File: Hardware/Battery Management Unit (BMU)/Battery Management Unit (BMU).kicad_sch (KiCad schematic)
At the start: 23 parts, among them J1 HIGH SIDE, J10 SHUNT, J11 ALERT, J12 CAN, J2 LOW SIDE, J3 POWER, J4 GPIO, J5 GND, J6 5V, J7 3V3, J8 FAULT, J9 I2C

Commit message: Both boards are now fully completed: the BMU and CMU.
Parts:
- TP1, TP10, TP11, TP2, TP3, TP4, TP5, TP6, TP7, TP8, TP9: symbol Connector:TestPoint_Small -> Connector:TestPoint_Square
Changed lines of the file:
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@@
 	)
 	(symbol
-		(lib_id "Connector:TestPoint_Small")
+		(lib_id "Connector:TestPoint_Square")
 		(at 240.03 153.67 0)
 		(unit 1)
@@
 		(in_pos_files yes)
 		(dnp no)
-		(fields_autoplaced yes)
 		(property "Reference" "TP3"
-			(at 241.3 152.3999 0)
+			(at 241.046 152.654 0)
 			(show_name no)
 			(do_not_autoplace no)
@@
 			)
 		)
-		(property "Datasheet" ""
+		(property "Datasheet" "~"
 			(at 245.11 153.67 0)
 			(hide yes)
@@
 	)
 	(symbol
-		(lib_id "Connector:TestPoint_Small")
+		(lib_id "Connector:TestPoint_Square")
 		(at 280.67 130.81 0)
 		(unit 1)
@@
 		(in_pos_files yes)
 		(dnp no)
-		(fields_autoplaced yes)
 		(property "Reference" "TP10"
-			(at 281.94 129.5399 0)
+			(at 281.686 129.794 0)
 			(show_name no)
 			(do_not_autoplace no)
@@
 			)
 		)
-		(property "Datasheet" ""
+		(property "Datasheet" "~"
 			(at 285.75 130.81 0)
 			(hide yes)
@@
 	)
 	(symbol
-		(lib_id "Connector:TestPoint_Small")
+		(lib_id "Connector:TestPoint_Square")
 		(at 279.4199 173.99 0)
 		(unit 1)
@@
 		(in_pos_files yes)
 		(dnp no)
-		(fields_autoplaced yes)
 		(property "Reference" "TP8"
-			(at 280.6899 172.7199 0)
+			(at 280.416 173.228 0)
 			(show_name no)
 			(do_not_autoplace no)
@@
 			)
 		)
-		(property "Datasheet" ""
+		(property "Datasheet" "~"
 			(at 284.4999 173.99 0)
 			(hide yes)
@@
 	)
 	(symbol
-		(lib_id "Connector:TestPoint_Small")
+		(lib_id "Connector:TestPoint_Square")
 		(at 279.4 165.1 0)
 		(unit 1)
@@
 		(in_pos_files yes)
 		(dnp no)
-		(fields_autoplaced yes)
 		(property "Reference" "TP6"
-			(at 280.67 163.8299 0)
+			(at 280.416 164.084 0)
 			(show_name no)
 			(do_not_autoplace no)
@@
 			)
 		)
-		(property "Datasheet" ""
+		(property "Datasheet" "~"
 			(at 284.48 165.1 0)
 			(hide yes)
@@
 	)
 	(symbol
-		(lib_id "Connector:TestPoint_Small")
+		(lib_id "Connector:TestPoint_Square")
 		(at 280.6355 135.89 0)
 		(unit 1)
@@
 		(in_pos_files yes)
 		(dnp no)
-		(fields_autoplaced yes)
 		(property "Reference" "TP9"
-			(at 281.9055 134.6199 0)
+			(at 281.94 134.874 0)
 			(show_name no)
 			(do_not_autoplace no)
@@
 			)
 		)
-		(property "Datasheet" ""
+		(property "Datasheet" "~"
 			(at 285.7155 135.89 0)
 			(hide yes)
@@
 	)
 	(symbol
-		(lib_id "Connector:TestPoint_Small")
+		(lib_id "Connector:TestPoint_Square")
 		(at 279.4 171.45 0)
 		(unit 1)
@@
 		(in_pos_files yes)
 		(dnp no)
-		(fields_autoplaced yes)
 		(property "Reference" "TP7"
-			(at 280.67 170.1799 0)
+			(at 280.416 170.434 0)
 			(show_name no)
 			(do_not_autoplace no)
@@
 			)
 		)
-		(property "Datasheet" ""
+		(property "Datasheet" "~"
 			(at 284.48 171.45 0)
 			(hide yes)
@@
 	)
 	(symbol
-		(lib_id "Connector:TestPoint_Small")
+		(lib_id "Connector:TestPoint_Square")
 		(at 279.3877 167.64 0)
 		(unit 1)
@@
 		(in_pos_files yes)
 		(dnp no)
-		(fields_autoplaced yes)
 		(property "Reference" "TP5"
-			(at 280.6577 166.3699 0)
+			(at 280.416 166.624 0)
 			(show_name no)
 			(do_not_autoplace no)
@@
 			)
 		)
-		(property "Datasheet" ""
+		(property "Datasheet" "~"
 			(at 284.4677 167.64 0)
 			(hide yes)
@@
 	)
 	(symbol
-		(lib_id "Connector:TestPoint_Small")
+		(lib_id "Connector:TestPoint_Square")
 		(at 240.03 144.78 0)
 		(unit 1)
@@
 		(in_pos_files yes)
 		(dnp no)
-		(fields_autoplaced yes)
 		(property "Reference" "TP2"
-			(at 241.3 143.5099 0)
+			(at 241.3 143.764 0)
 			(show_name no)
 			(do_not_autoplace no)
@@
 			)
 		)
-		(property "Datasheet" ""
+		(property "Datasheet" "~"
 			(at 245.11 144.78 0)
 			(hide yes)
@@
 	)
 	(symbol
-		(lib_id "Connector:TestPoint_Small")
+		(lib_id "Connector:TestPoint_Square")
 		(at 280.67 133.35 0)
 		(unit 1)
@@
 		(in_pos_files yes)
 		(dnp no)
-		(fields_autoplaced yes)
 		(property "Reference" "TP11"
-			(at 281.94 132.0799 0)
+			(at 281.686 132.334 0)
 			(show_name no)
 			(do_not_autoplace no)
@@
 			)
 		)
-		(property "Datasheet" ""
+		(property "Datasheet" "~"
 			(at 285.75 133.35 0)
 			(hide yes)
@@
 	)
 	(symbol
-		(lib_id "Connector:TestPoint_Small")
+		(lib_id "Connector:TestPoint_Square")
 		(at 240.03 142.24 0)
 		(unit 1)
@@
 		(in_pos_files yes)
 		(dnp no)
-		(fields_autoplaced yes)
 		(property "Reference" "TP1"
-			(at 241.3 140.9699 0)
+			(at 241.3 140.97 0)
 			(show_name no)
 			(do_not_autoplace no)
@@
 			)
 		)
-		(property "Datasheet" ""
+		(property "Datasheet" "~"
 			(at 245.11 142.24 0)
 			(hide yes)
@@
 	)
 	(symbol
-		(lib_id "Connector:TestPoint_Small")
+		(lib_id "Connector:TestPoint_Square")
 		(at 279.3064 177.8 0)
 		(unit 1)
@@
 		(in_pos_files yes)
 		(dnp no)
-		(fields_autoplaced yes)
 		(property "Reference" "TP4"
-			(at 280.5764 176.5299 0)
+			(at 280.162 176.784 0)
 			(show_name no)
 			(do_not_autoplace no)
@@
 			)
 		)
-		(property "Datasheet" ""
+		(property "Datasheet" "~"
 			(at 284.3864 177.8 0)
 			(hide yes)

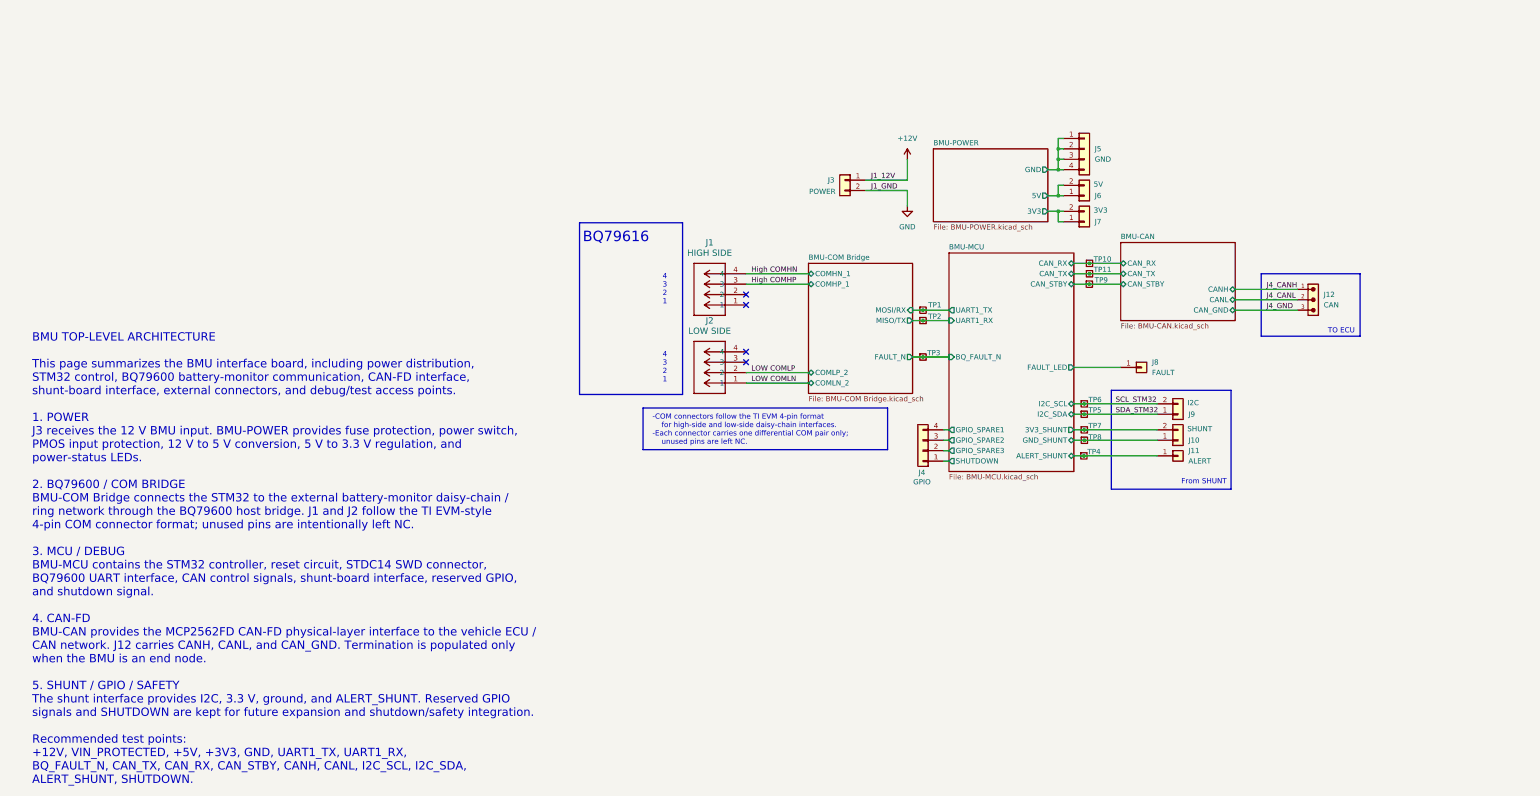
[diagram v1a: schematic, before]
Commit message: Schematic polish -- fixed to best standards, cleaned up for ERCs, etc
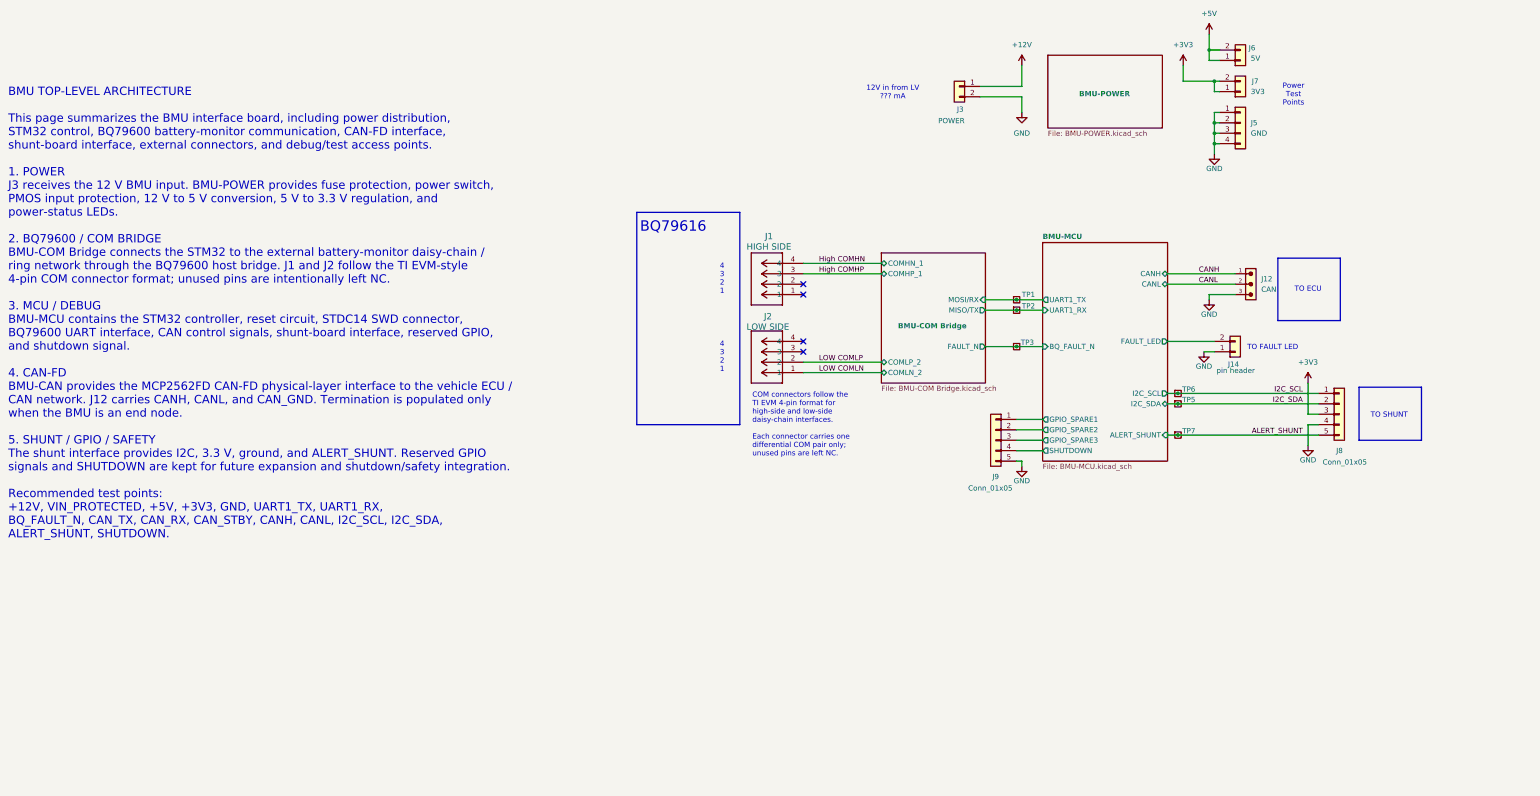
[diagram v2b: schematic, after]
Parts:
- removed J10: SHUNT, Connector_PinHeader_2.54mm:PinHeader_1x02_P2.54mm_Vertical, symbol Connector_Generic:Conn_01x02
- removed J11: ALERT, Connector_PinHeader_2.54mm:PinHeader_1x01_P2.54mm_Vertical, symbol Connector_Generic:Conn_01x01
- removed J4: GPIO, Connector_PinHeader_2.54mm:PinHeader_1x04_P2.54mm_Vertical, symbol Connector_Generic:Conn_01x04
- removed J8: FAULT, Connector_PinHeader_2.54mm:PinHeader_1x01_P2.54mm_Vertical, symbol Connector_Generic:Conn_01x01
- removed J9: I2C, Connector_PinHeader_2.54mm:PinHeader_1x02_P2.54mm_Vertical, symbol Connector_Generic:Conn_01x02
- removed TP10, TP11, TP4, TP8, TP9: TestPoint_Small, TestPoint:TestPoint_THTPad_D1.5mm_Drill0.7mm, symbol Connector:TestPoint_Square
- added J14: pin header, Connector_PinHeader_2.54mm:PinHeader_1x02_P2.54mm_Vertical, symbol Connector_Generic:Conn_01x02
- added J8, J9: Conn_01x05, symbol Connector_Generic:Conn_01x05
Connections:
- net BMU-POWER/GND is gone; now on net GND: J5.1 (Pin_1), J5.2 (Pin_2), J5.3 (Pin_3), J5.4 (Pin_4)
- net J4_GND is gone; now on net GND: J12.3
- net BMU-MCU/FAULT_LED: now also J14.2 (Pin_2)
- net BMU-MCU/GPIO_SPARE1: now also J9.1 (Pin_1)
- net BMU-MCU/GPIO_SPARE2: now also J9.2 (Pin_2)
- net BMU-MCU/GPIO_SPARE3: now also J9.3 (Pin_3)
- net BMU-MCU/SHUTDOWN: now also J9.4 (Pin_4)
- net GND: now also J14.1 (Pin_1), J8.4 (Pin_4), J9.5 (Pin_5)
- net BMU-MCU/3V3_SHUNT renamed ALERT_SHUNT
- net ALERT_SHUNT: now also J8.5 (Pin_5)
- net BMU-POWER/3V3 renamed +3V3
- net +3V3: now also J8.3 (Pin_3)
- net BMU-POWER/5V renamed +5V
- net J4_CANH renamed CANH
- net J4_CANL renamed CANL
- net SCL_STM32 renamed I2C_SCL
- net I2C_SCL: now also J8.1 (Pin_1)
- net SDA_STM32 renamed I2C_SDA
- net I2C_SDA: now also J8.2 (Pin_2)
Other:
- removed sheet BMU-CAN
- sheet BMU-MCU ports: added CANH, CANL; removed 3V3_SHUNT, CAN_RX, CAN_STBY, CAN_TX, GND_SHUNT
- sheet BMU-POWER ports: added none; removed 3V3, 5V, GND
- note added: "12V in from LV ??? mA"
- note added: "COM connectors follow the TI EVM 4-pin format for high-side and low-side daisy-chain interfaces. Each connector carries one differential COM pair only; unused pins are left NC."
- note added: "Power Test Points"
- note added: "TO FAULT LED"
- note added: "TO SHUNT"
- note removed: "-COM connectors follow the TI EVM 4-pin format for high-side and low-side daisy-chain interfaces. -Each connector carries one differential COM pair only; unused pins are left NC."
- note removed: "From SHUNT"
- moved on the sheet: J1, J12, J2, J3, J5, J6, J7, TP1, TP2, TP3, TP5, TP6

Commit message: update libraries+bmu
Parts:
- J1, J2: footprint 705510038:CONN_70551-xxxx_04_MOL -> Footprints:705510038
- J10: renamed from J8; value Conn_01x05 -> SHUNT; footprint (none) -> Connector_PinHeader_2.54mm:PinHeader_1x05_P2.54mm_Vertical
- J4: renamed from J9; value Conn_01x05 -> GPIO; footprint (none) -> Connector_PinHeader_2.54mm:PinHeader_1x05_P2.54mm_Vertical
- J9: renamed from J12; footprint 691382000003:691382000003 -> Footprints:691382000003
- renumbered J6 to J5, J7 to J6, J5 to J7, J14 to J8, TP5 to TP4, TP6 to TP5, TP7 to TP6
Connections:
- net +3V3: now also J10.1 (Pin_1); no longer J10.3 (Pin_3)
- net ALERT_SHUNT: now also J10.4 (Pin_4); no longer J10.5 (Pin_5)
- net GND: now also J10.5 (Pin_5); no longer J10.4 (Pin_4)
- net I2C_SCL: now also J10.3 (Pin_3); no longer J10.1 (Pin_1)
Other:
- moved on the sheet: J1, J10, J2, J3, J4, J5, J6, J7, J8, J9, TP1, TP2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

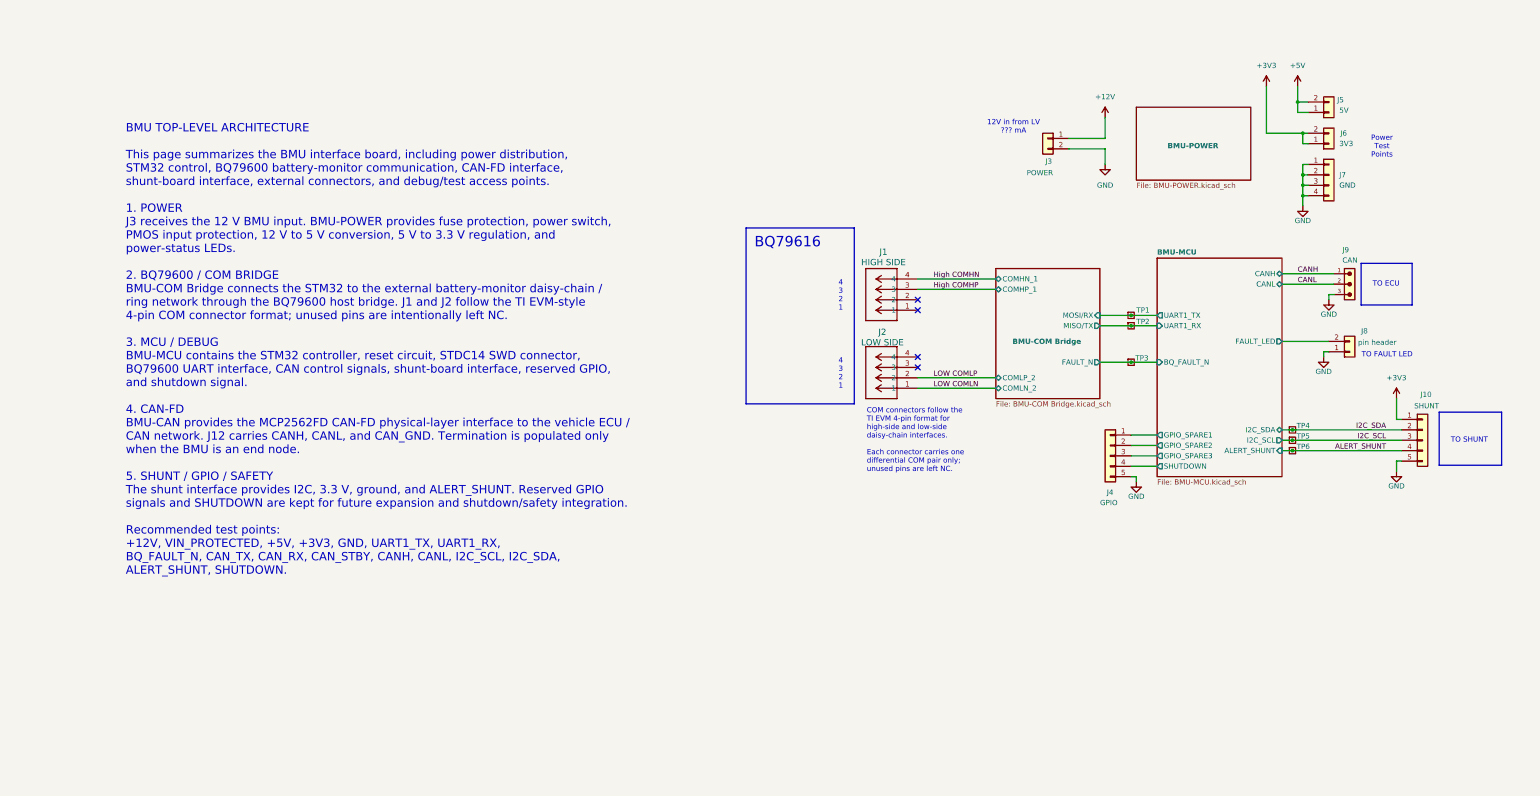
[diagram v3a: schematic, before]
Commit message: Schematic cleanup; lots of missing library files
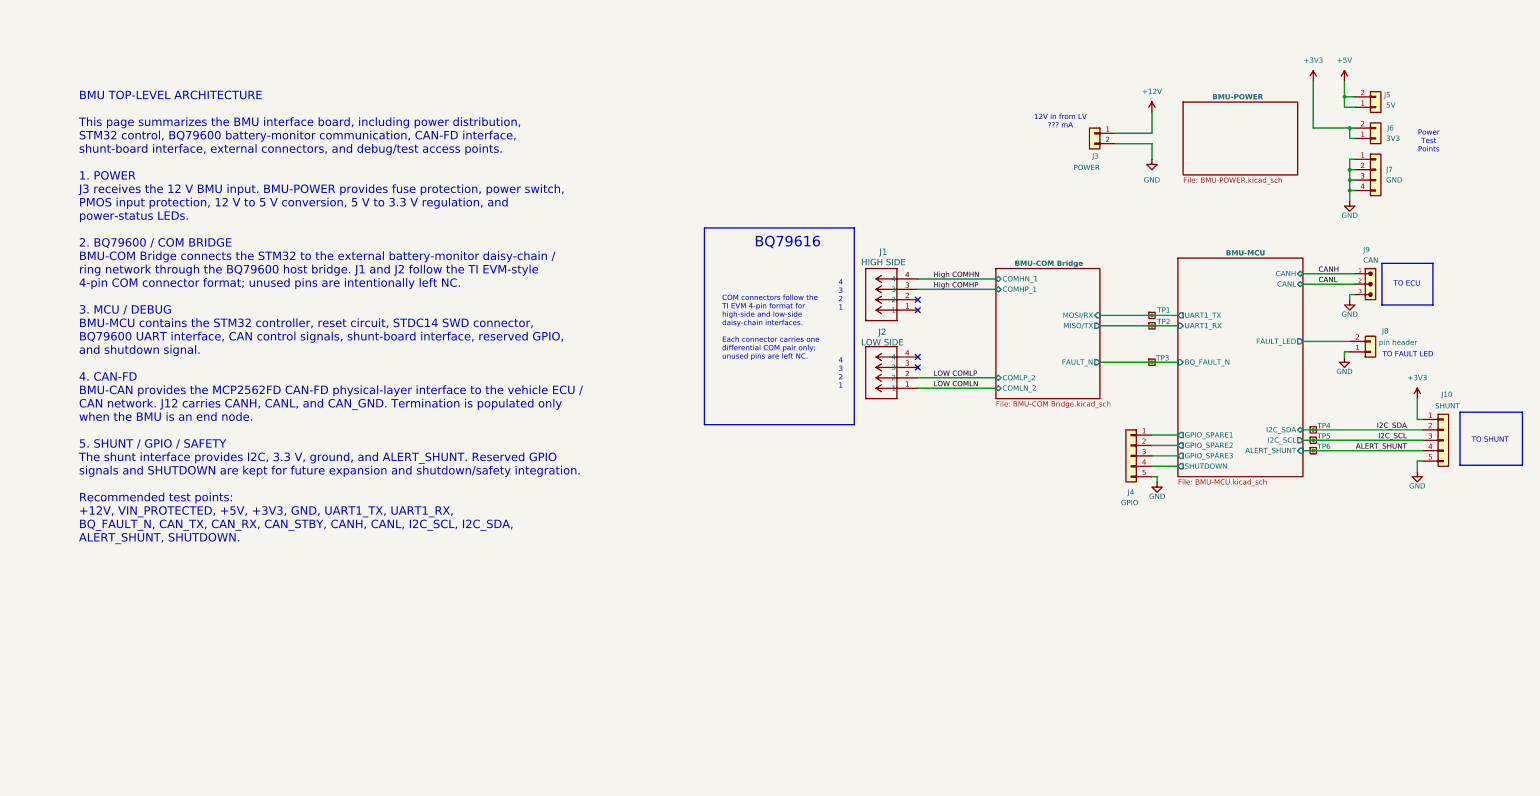
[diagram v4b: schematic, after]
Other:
- moved on the sheet: J10, J3, J4, J5, J6, J7, J8, J9, TP1, TP2, TP3, TP4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

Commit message: Fixed all missing symbol and footprint libraries
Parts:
- J1, J2: symbol 70551-0038:705510038 -> 705510038:705510038
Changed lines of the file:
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@@
 	)
 	(symbol
-		(lib_id "70551-0038:705510038")
+		(lib_id "705510038:705510038")
 		(at 238.76 142.24 180)
 		(unit 1)
@@
 	)
 	(symbol
-		(lib_id "70551-0038:705510038")
+		(lib_id "705510038:705510038")
 		(at 238.76 161.29 180)
 		(unit 1)
